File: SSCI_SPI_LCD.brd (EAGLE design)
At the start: 110 x 100 mm, 33 parts, among them IC3 74LVC541_RGY, X1 PHA-1X08SG, X2 PHA-1X08SG

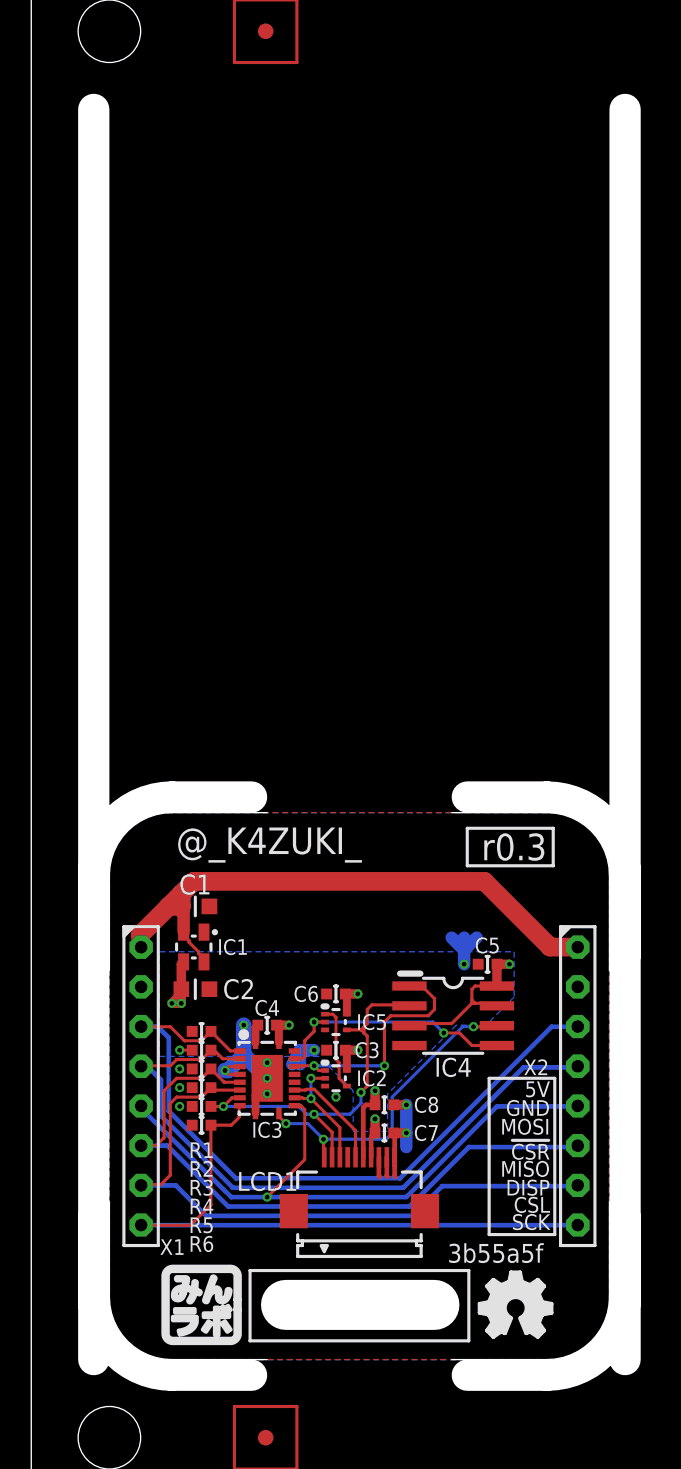
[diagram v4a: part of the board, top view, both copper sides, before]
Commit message: R3 connected to 3.3V (to pull up DISP pin)
- left-top corner(at LCD top view) has key-hole
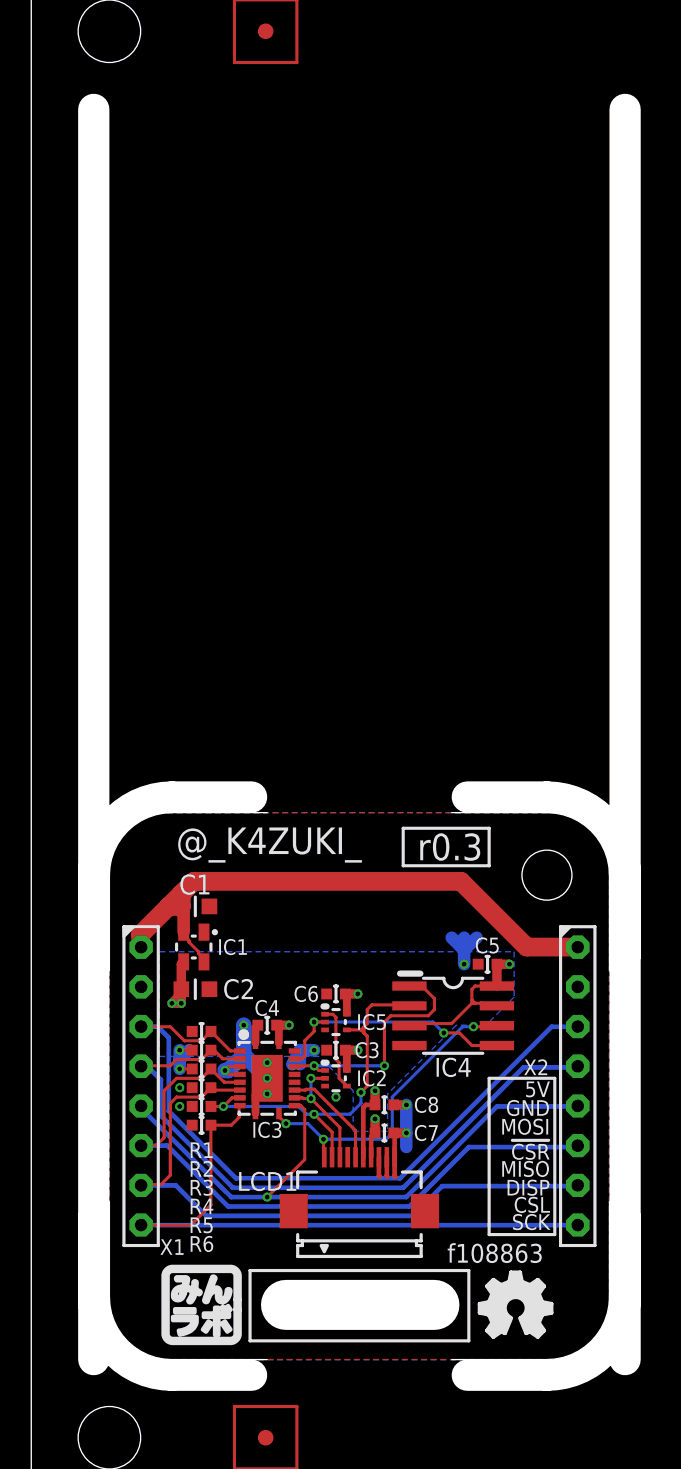
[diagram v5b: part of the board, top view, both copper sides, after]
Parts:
- GIT1: value 3b55a5f -> f108863
- P2: device mylib:PCB_CORNER_NH -> mylib:PCB_CORNER
- moved ICON1 4.10 mm to (26.9, 42.8)
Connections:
- net 3.3V: now also R3.1
- net GND: no longer R3.1
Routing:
- net 3.3V: track 30.0 -> 32.9 mm, vias 9 -> 10
- net GND: vias 13 -> 12
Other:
- outline, holes or cut-outs redrawn
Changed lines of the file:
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@@
 <layer number="35" name="tGlue" color="7" fill="4" visible="no" active="yes"/>
 <layer number="36" name="bGlue" color="7" fill="5" visible="no" active="yes"/>
-<layer number="37" name="tTest" color="7" fill="1" visible="yes" active="yes"/>
+<layer number="37" name="tTest" color="7" fill="1" visible="no" active="yes"/>
 <layer number="38" name="bTest" color="7" fill="1" visible="no" active="yes"/>
 <layer number="39" name="tKeepout" color="4" fill="11" visible="no" active="yes"/>
@@
 <dimension x1="71" y1="0" x2="39" y2="0" x3="55" y3="-6.9" textsize="1.778" layer="47"/>
 <dimension x1="105" y1="0" x2="73" y2="0" x3="89" y3="-6.9" textsize="1.778" layer="47"/>
-<wire x1="4" y1="10" x2="4" y2="19.1" width="2" layer="46"/>
-<wire x1="4" y1="19.1" x2="4" y2="90" width="2" layer="46"/>
+<wire x1="4" y1="10" x2="4" y2="90" width="2" layer="46"/>
 <wire x1="38" y1="10" x2="38" y2="90" width="2" layer="46"/>
 <wire x1="72" y1="10" x2="72" y2="90" width="2" layer="46"/>
@@
 <attribute name="NOT_COMPONENT" value="YES" x="33" y="14" size="1.778" layer="27" display="off"/>
 </element>
-<element name="P2" library="mylib" package="PCB_CORNER_NH" value="" x="33" y="41" smashed="yes" rot="R90">
+<element name="P2" library="mylib" package="PCB_CORNER" value="" x="33" y="41" smashed="yes" rot="R90">
 <attribute name="NOT_COMPONENT" value="YES" x="33" y="41" size="1.778" layer="27" rot="R90" display="off"/>
 </element>
@@
 <attribute name="NOT_COMPONENT" value="YES" x="9" y="14" size="1.778" layer="27" rot="R270" display="off"/>
 </element>
-<element name="GIT1" library="git-revision" package="GIT-REVISION_1.2" value="3b55a5f" x="29.7" y="16.8">
+<element name="GIT1" library="git-revision" package="GIT-REVISION_1.2" value="f108863" x="29.7" y="16.8">
 <attribute name="NOT_COMPONENT" value="YES" x="29.7" y="16.8" size="1.778" layer="27" display="off"/>
 </element>
-<element name="ICON1" library="mylib" package="ICON_REVISION1.7" value="r0.3" x="31" y="42.8">
-<attribute name="NOT_COMPONENT" value="YES" x="31" y="42.8" size="1.778" layer="27" display="off"/>
+<element name="ICON1" library="mylib" package="ICON_REVISION1.7" value="r0.3" x="26.9" y="42.8">
+<attribute name="NOT_COMPONENT" value="YES" x="26.9" y="42.8" size="1.778" layer="27" display="off"/>
 </element>
 <element name="X1" library="mylib" package="PHA-1X08SG" value="PHA-1X08SG" x="7.03" y="27.5" smashed="yes" rot="R90">
@@
 <contactref element="R1" pad="1"/>
 <contactref element="R5" pad="1"/>
-<contactref element="R3" pad="1"/>
 <contactref element="R4" pad="1"/>
 <contactref element="R6" pad="1"/>
@@
 <via x="24" y="24.5" extent="1-16" drill="0.3"/>
 <via x="9.5" y="26.2" extent="1-16" drill="0.3"/>
-<via x="9.5" y="28.6" extent="1-16" drill="0.3"/>
 <polygon width="0.2" layer="16" rank="2">
 <vertex x="5" y="45"/>
@@
 <wire x1="9.6" y1="39" x2="9.6" y2="39.8" width="1.2" layer="1"/>
 <wire x1="9.6" y1="39.8" x2="10.4" y2="40.6" width="1.2" layer="1"/>
-<wire x1="10.4" y1="40.6" x2="29" y2="40.6" width="1.2" layer="1"/>
-<wire x1="33.2" y1="36.4" x2="29" y2="40.6" width="1.2" layer="1"/>
+<wire x1="10.4" y1="40.6" x2="27.5" y2="40.6" width="1.2" layer="1"/>
+<wire x1="31.7" y1="36.4" x2="27.5" y2="40.6" width="1.2" layer="1"/>
 <wire x1="8.8" y1="39" x2="9.6" y2="39.8" width="1.2" layer="1"/>
 <wire x1="8.8" y1="39" x2="9.1" y2="39" width="0.6" layer="1"/>
 <wire x1="9.1" y1="39" x2="9.7" y2="38.4" width="0.6" layer="1"/>
-<wire x1="33.2" y1="36.4" x2="34.96" y2="36.4" width="1.2" layer="1"/>
+<wire x1="31.7" y1="36.4" x2="34.96" y2="36.4" width="1.2" layer="1"/>
 <wire x1="34.96" y1="36.4" x2="34.97" y2="36.39" width="1.2" layer="1"/>
 <wire x1="7" y1="37.2" x2="7" y2="36.4" width="1.2" layer="1"/>
@@
 <wire x1="9" y1="32.8" x2="9.6" y2="33.4" width="0.6" layer="1"/>
 <wire x1="28.2" y1="33" x2="28.4" y2="32.8" width="0.2" layer="1"/>
+<contactref element="R3" pad="1"/>
+<via x="9.5" y="28.6" extent="1-16" drill="0.3"/>
+<wire x1="9.5" y1="28.6" x2="10.3" y2="28.6" width="0.2" layer="1"/>
+<wire x1="9.5" y1="28.6" x2="9.5" y2="29.2" width="0.8" layer="16"/>
+<wire x1="9.5" y1="29.2" x2="9.5" y2="29.8" width="0.8" layer="16"/>
+<wire x1="9.5" y1="29.2" x2="10.1" y2="29.8" width="0.8" layer="16"/>
 </signal>
 <signal name="N$2">

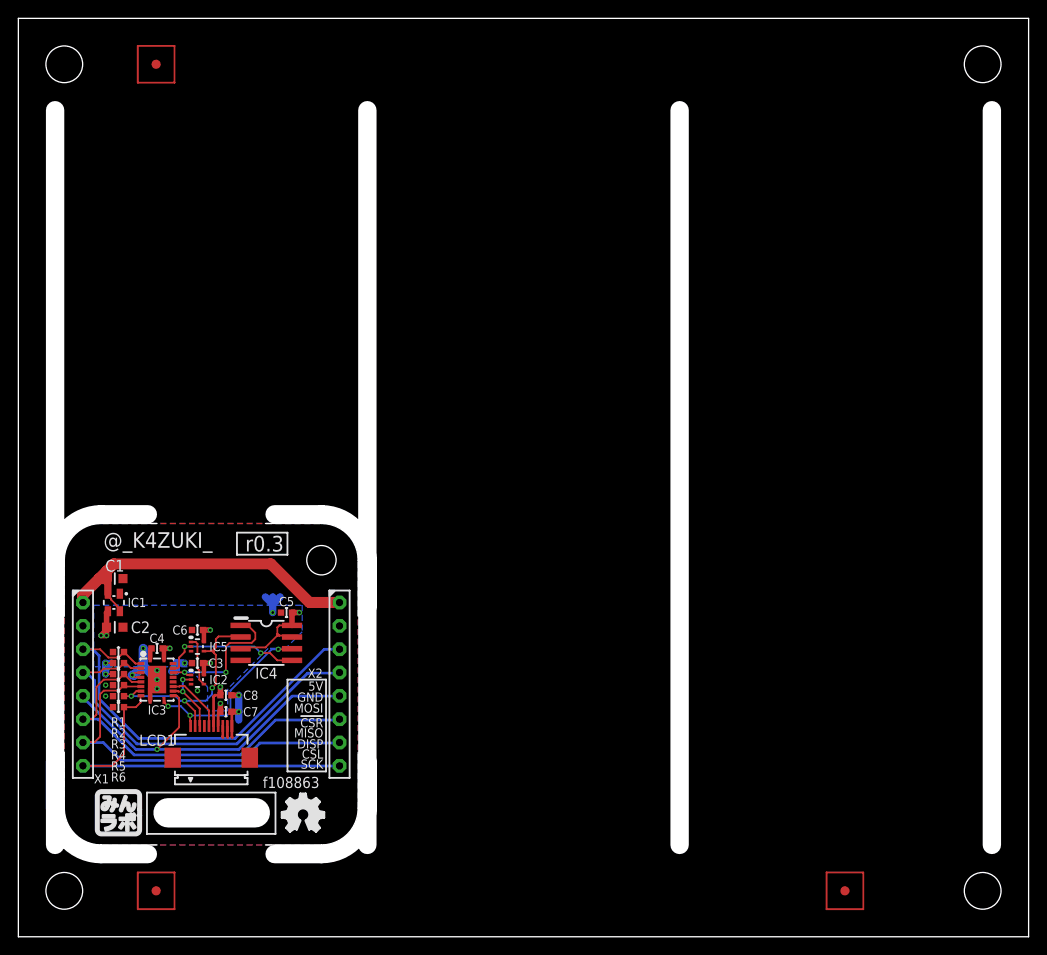
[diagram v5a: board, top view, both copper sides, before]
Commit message: keyhole replaced by milling
X2 note is tPlace layer
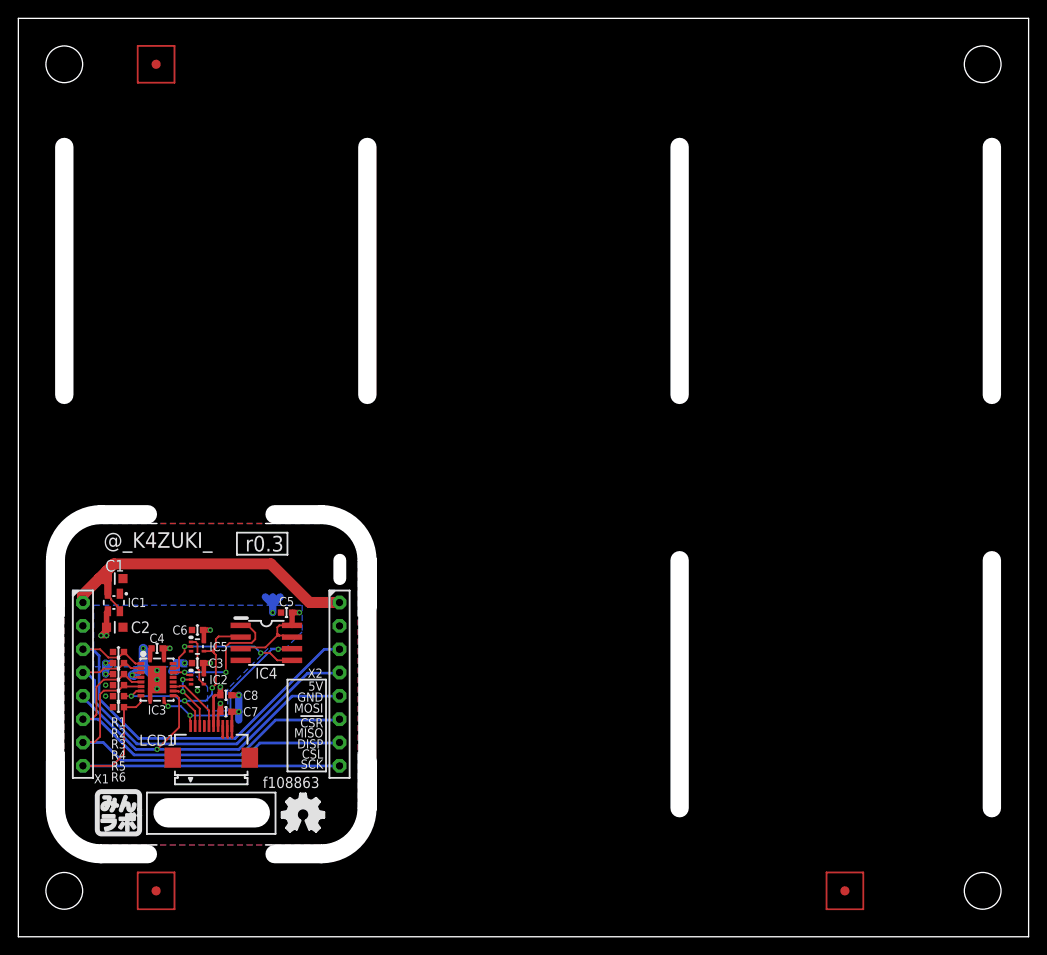
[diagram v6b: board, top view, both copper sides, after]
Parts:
- P2: device mylib:PCB_CORNER -> mylib:PCB_CORNER_NH
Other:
- outline, holes or cut-outs redrawn
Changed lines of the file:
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@@
 <dimension x1="71" y1="0" x2="39" y2="0" x3="55" y3="-6.9" textsize="1.778" layer="47"/>
 <dimension x1="105" y1="0" x2="73" y2="0" x3="89" y3="-6.9" textsize="1.778" layer="47"/>
-<wire x1="4" y1="10" x2="4" y2="90" width="2" layer="46"/>
-<wire x1="38" y1="10" x2="38" y2="90" width="2" layer="46"/>
-<wire x1="72" y1="10" x2="72" y2="90" width="2" layer="46"/>
-<wire x1="106" y1="10" x2="106" y2="90" width="2" layer="46"/>
+<wire x1="4" y1="14" x2="4" y2="41" width="2" layer="46"/>
 <wire x1="112" y1="10" x2="0" y2="10" width="0.3" layer="102"/>
 <wire x1="112" y1="45" x2="0" y2="45" width="0.3" layer="102"/>
@@
 <dimension x1="7.03" y1="27.5" x2="5" y2="27.5" x3="6.015" y3="2.9" textsize="1.778" layer="47" dtype="horizontal" visible="yes"/>
 <dimension x1="34.97" y1="27.5" x2="37" y2="27.5" x3="35.985" y3="2.9" textsize="1.778" layer="47" dtype="horizontal" visible="yes"/>
-<text x="33.2" y="27.3" size="1" layer="25" ratio="20" rot="R180" align="center-left">5V</text>
-<text x="33.2" y="26.1" size="1" layer="25" ratio="20" rot="R180" align="center-left">GND</text>
-<text x="33.2" y="24.9" size="1" layer="25" ratio="20" rot="R180" align="center-left">MOSI</text>
-<text x="33.2" y="23.3" size="1" layer="25" ratio="20" rot="R180" align="center-left">!CSR!</text>
-<text x="33.2" y="22.2" size="1" layer="25" ratio="20" rot="R180" align="center-left">MISO</text>
-<text x="33.2" y="21" size="1" layer="25" ratio="20" rot="R180" align="center-left">DISP</text>
-<text x="33.2" y="19.9" size="1" layer="25" ratio="20" rot="R180" align="center-left">CSL</text>
-<text x="33.2" y="18.8" size="1" layer="25" ratio="20" rot="R180" align="center-left">SCK</text>
+<text x="33.2" y="27.3" size="1" layer="21" ratio="20" rot="R180" align="center-left">5V</text>
+<text x="33.2" y="26.1" size="1" layer="21" ratio="20" rot="R180" align="center-left">GND</text>
+<text x="33.2" y="24.9" size="1" layer="21" ratio="20" rot="R180" align="center-left">MOSI</text>
+<text x="33.2" y="23.3" size="1" layer="21" ratio="20" rot="R180" align="center-left">!CSR!</text>
+<text x="33.2" y="22.2" size="1" layer="21" ratio="20" rot="R180" align="center-left">MISO</text>
+<text x="33.2" y="21" size="1" layer="21" ratio="20" rot="R180" align="center-left">DISP</text>
+<text x="33.2" y="19.9" size="1" layer="21" ratio="20" rot="R180" align="center-left">CSL</text>
+<text x="33.2" y="18.8" size="1" layer="21" ratio="20" rot="R180" align="center-left">SCK</text>
 <dimension x1="5" y1="10" x2="5" y2="45" x3="5" y3="27.5" textsize="1.778" layer="47" visible="yes"/>
 <wire x1="33.5" y1="28" x2="29.3" y2="28" width="0.2" layer="21"/>
@@
 <dimension x1="110" y1="0" x2="105" y2="0" x3="107.5" y3="-6.9" textsize="1.778" layer="47"/>
 <rectangle x1="5" y1="10" x2="37" y2="45" layer="37"/>
+<wire x1="38" y1="14" x2="38" y2="41" width="2" layer="46"/>
+<wire x1="38" y1="59" x2="38" y2="86" width="2" layer="46"/>
+<wire x1="72" y1="59" x2="72" y2="86" width="2" layer="46"/>
+<wire x1="72" y1="14" x2="72" y2="41" width="2" layer="46"/>
+<wire x1="106" y1="14" x2="106" y2="41" width="2" layer="46"/>
+<wire x1="106" y1="59" x2="106" y2="86" width="2" layer="46"/>
+<wire x1="5" y1="59" x2="5" y2="86" width="2" layer="46"/>
+<wire x1="35" y1="41" x2="35" y2="39" width="1.4" layer="46"/>
+<wire x1="35" y1="41" x2="35" y2="39" width="2" layer="41"/>
+<wire x1="35" y1="41" x2="35" y2="39" width="2" layer="42"/>
 </plain>
 <attributes>
@@
 <attribute name="NOT_COMPONENT" value="YES" x="33" y="14" size="1.778" layer="27" display="off"/>
 </element>
-<element name="P2" library="mylib" package="PCB_CORNER" value="" x="33" y="41" smashed="yes" rot="R90">
+<element name="P2" library="mylib" package="PCB_CORNER_NH" value="" x="33" y="41" smashed="yes" rot="R90">
 <attribute name="NOT_COMPONENT" value="YES" x="33" y="41" size="1.778" layer="27" rot="R90" display="off"/>
 </element>

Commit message: 8c37b00 panelized
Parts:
- GIT1: value f108863 -> 8c37b00
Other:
- outline, holes or cut-outs redrawn
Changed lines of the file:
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@@
 <dimension x1="110" y1="0" x2="105" y2="0" x3="107.5" y3="-6.9" textsize="1.778" layer="47"/>
 <rectangle x1="5" y1="10" x2="37" y2="45" layer="37"/>
-<wire x1="38" y1="14" x2="38" y2="41" width="2" layer="46"/>
-<wire x1="38" y1="59" x2="38" y2="86" width="2" layer="46"/>
-<wire x1="72" y1="59" x2="72" y2="86" width="2" layer="46"/>
-<wire x1="72" y1="14" x2="72" y2="41" width="2" layer="46"/>
+<wire x1="38" y1="14" x2="38" y2="41" width="2" layer="51"/>
+<wire x1="38" y1="59" x2="38" y2="86" width="2" layer="51"/>
+<wire x1="72" y1="59" x2="72" y2="86" width="2" layer="51"/>
+<wire x1="72" y1="14" x2="72" y2="41" width="2" layer="51"/>
 <wire x1="106" y1="14" x2="106" y2="41" width="2" layer="46"/>
 <wire x1="106" y1="59" x2="106" y2="86" width="2" layer="46"/>
-<wire x1="5" y1="59" x2="5" y2="86" width="2" layer="46"/>
+<wire x1="4" y1="59" x2="4" y2="86" width="2" layer="51"/>
 <wire x1="35" y1="41" x2="35" y2="39" width="1.4" layer="46"/>
 <wire x1="35" y1="41" x2="35" y2="39" width="2" layer="41"/>
@@
 <attribute name="NOT_COMPONENT" value="YES" x="9" y="14" size="1.778" layer="27" rot="R270" display="off"/>
 </element>
-<element name="GIT1" library="git-revision" package="GIT-REVISION_1.2" value="f108863" x="29.7" y="16.8">
+<element name="GIT1" library="git-revision" package="GIT-REVISION_1.2" value="8c37b00" x="29.7" y="16.8">
 <attribute name="NOT_COMPONENT" value="YES" x="29.7" y="16.8" size="1.778" layer="27" display="off"/>
 </element>
